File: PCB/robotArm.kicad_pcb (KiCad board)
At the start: 2 copper layers, 85 parts, among them J1 Motor_eje_X, J10 Gripper, J11 Conector Auxiliar 2, J12 5v, J13 End-Stop-X, J14 End-Stop-Y, J15 End-Stop-Z, J16 jumperLed5v, J17 Conector Auxiliar 1, J18 jumperLedVbat, J19 Vbat, J2 3.3v, J20 jumperLedVcc, J21 Vcc, J3 Motor_eje_Y, J4 Motor_eje_Z, J5 micro pasos X, J6 micro pasos Y, J7 micro pasos Z, J8 Conector I2C, J9 jumperLed3.3v, Q1 BC558, Q2 BC558, Q3 BC558, SW1 SW_Push, U1 YAAJ_BluePill, U2 LM7805_TO220, U3 LM317_TO-220

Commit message: PCB pull from master (#12)
* Update README.md

Se agregó descripción,  introducción y fuentes.

* Se consiguió una primera versión de Eje-Stop funcional

* Se inició una interfaz en python sencilla para la comunicación con el robot

* Se comenzó con conexión USB

* Se agregó LCD i2c y lógica de CDC

* update interface

* Se actualizaron los cambios

* return 2025

* El homming funciona!

* modo ejecución v1.0 funciona correctamente

* Se avanzo interfaz 3 modos funcionales v1.0

* actualizaciones en la interfaz

* Recuperando cambios del stash

* Se recuperaron las modificaciones de interfaz

* Se agregó leds en interfaz, botón de limpiar aprendizaje, se arregló configuración de velocidad en bluepill

* readme de stm32

* Se actualizo interfaz v1.0

* Se agregó rampa de velocidad

---------

Co-authored-by: Francisco Cano <100385537+FranciscoCano2@users.noreply.github.com>
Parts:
- removed C1: 103, Capacitor_THT:C_Disc_D8.0mm_W2.5mm_P5.00mm
- removed C6: 470uF, Capacitor_THT:CP_Radial_D8.0mm_P3.80mm
- removed D12: LED_Vbat, LED_THT:LED_D5.0mm
- removed D13, D4, D5, D6, D7, D8, D9: 1N4007, Diode_THT:D_DO-41_SOD81_P10.16mm_Horizontal
- removed J19: Vbat, TerminalBlock:TerminalBlock_bornier-2_P5.08mm
- removed R10: 220, Resistor_THT:R_Axial_DIN0207_L6.3mm_D2.5mm_P10.16mm_Horizontal
- added C19: 103, Capacitor_THT:C_Disc_D8.0mm_W2.5mm_P5.00mm, F.Cu at (166.5, 100.0)
- added C20: 103, Capacitor_THT:C_Disc_D8.0mm_W2.5mm_P5.00mm, F.Cu at (179.0, 98.0)
- added H1: MountingHole, MountingHole:MountingHole_3.2mm_M3_DIN965, F.Cu at (258.5, 42.5)
- added H2: MountingHole, MountingHole:MountingHole_3.2mm_M3_DIN965, F.Cu at (165.0, 40.5)
- added H3: MountingHole, MountingHole:MountingHole_3.2mm_M3_DIN965, F.Cu at (258.5, 134.0)
- added H4: MountingHole, MountingHole:MountingHole_3.2mm_M3_DIN965, F.Cu at (166.0, 135.0)
- added R16: 1k, Resistor_THT:R_Axial_DIN0207_L6.3mm_D2.5mm_P10.16mm_Horizontal, F.Cu at (239.3, 101.8)
- added R17: 1k, Resistor_THT:R_Axial_DIN0207_L6.3mm_D2.5mm_P10.16mm_Horizontal, F.Cu at (235.7, 101.7)
- added R18: 1k, Resistor_THT:R_Axial_DIN0207_L6.3mm_D2.5mm_P10.16mm_Horizontal, F.Cu at (232.1, 101.7)
- added R19: 10k, Resistor_THT:R_Axial_DIN0207_L6.3mm_D2.5mm_P10.16mm_Horizontal, F.Cu at (173.1, 93.0)
- added SW2: STOP_EM, Button_Switch_THT:SW_PUSH_6mm_H5mm, F.Cu at (166.6, 106.2)
- C11, C8: value 470uF -> 10uF
- C5: value 47uF -> 10uF
- D1: value 1N4007 -> LED_Home; footprint Diode_THT:D_DO-41_SOD81_P10.16mm_Horizontal -> LED_THT:LED_D5.0mm
- D2: value 1N4007 -> LED_Wait; footprint Diode_THT:D_DO-41_SOD81_P10.16mm_Horizontal -> LED_THT:LED_D5.0mm
- D3: value 1N4007 -> LED_Finish; footprint Diode_THT:D_DO-41_SOD81_P10.16mm_Horizontal -> LED_THT:LED_D5.0mm
- J12, J2: footprint TerminalBlock:TerminalBlock_bornier-2_P5.08mm -> TerminalBlock_Phoenix:TerminalBlock_Phoenix_PT-1,5-2-5.0-H_1x02_P5.00mm_Horizontal
- J18: value jumperLedVbat -> Pulsador Externo; footprint Connector_PinHeader_2.54mm:PinHeader_2x01_P2.54mm_Vertical -> Connector_PinHeader_2.54mm:PinHeader_1x02_P2.54mm_Vertical
- J21: footprint TerminalBlock:TerminalBlock_bornier-2_P5.08mm -> TerminalBlock_Phoenix:TerminalBlock_Phoenix_MKDS-1,5-2_1x02_P5.00mm_Horizontal
- J5, J6, J7: footprint Connector_PinSocket_2.54mm:PinSocket_2x03_P2.54mm_Vertical -> Connector_PinHeader_2.54mm:PinHeader_2x03_P2.54mm_Vertical
- R12, R13, R7: value 10k -> 47k
- R2, R3, R4: value 10k -> 4.7k
- SW1: value SW_Push -> RESET
- moved D1 174.9 mm to (229.9, 132.3), turned to 0 degrees
- moved D2 148.2 mm to (230.0, 118.1), turned to 0 degrees
- moved J9 128.1 mm to (256.1, 119.8), turned to 180 degrees
- moved R5 127.0 mm to (182.0, 69.7), turned to -90 degrees
- moved D3 124.6 mm to (229.9, 125.4), turned to 0 degrees
- moved R7 122.0 mm to (206.4, 128.3)
- moved D10 121.8 mm to (250.5, 120.5), turned to -90 degrees
- moved R1 121.0 mm to (252.7, 116.8)
- moved C5 120.4 mm to (244.5, 123.1)
- moved C7 114.9 mm to (249.9, 127.2), turned to -90 degrees
- moved C9 110.8 mm to (223.6, 133.7)
- moved J16 109.1 mm to (214.3, 126.7)
- moved J2 108.8 mm to (240.3, 132.0), turned to 0 degrees
- moved R2 108.2 mm to (192.0, 59.8)
- moved D11 107.6 mm to (212.8, 121.4)
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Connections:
- A1 pad 10: Net-(A1-Pad10) -> Net-(A1-MS1)
- A1 pad 12: Net-(A1-Pad12) -> Net-(A1-MS3)
- A1 pad 13: Net-(A1-Pad13) -> Net-(A1-~{RESET})
- A1 pad 14: Net-(A1-Pad14) -> Net-(A1-~{RESET})
- A1 pad 9: Net-(A1-Pad9) -> EnableMotor
- A2 pad 10: Net-(A2-Pad10) -> Net-(A2-MS1)
- A2 pad 12: Net-(A2-Pad12) -> Net-(A2-MS3)
- A2 pad 13: Net-(A2-Pad13) -> Net-(A2-~{RESET})
- A2 pad 14: Net-(A2-Pad14) -> Net-(A2-~{RESET})
- A2 pad 9: Net-(A2-Pad9) -> EnableMotor
- A3 pad 10: Net-(A3-Pad10) -> Net-(A3-MS1)
- A3 pad 12: Net-(A3-Pad12) -> Net-(A3-MS3)
- A3 pad 13: Net-(A3-Pad13) -> Net-(A3-~{RESET})
- A3 pad 14: Net-(A3-Pad14) -> Net-(A3-~{RESET})
- A3 pad 9: Net-(A3-Pad9) -> EnableMotor
- D1 pad 1: Net-(A1-Pad9) -> GNDREF
- D1 pad 2: EnableMotor -> Net-(D1-A)
- D18 pad 2: Net-(D18-Pad2) -> Net-(D18-A)
- D2 pad 1: Net-(A2-Pad9) -> GNDREF
- D2 pad 2: EnableMotor -> Net-(D2-A)
- D3 pad 1: Net-(A3-Pad9) -> GNDREF
- D3 pad 2: EnableMotor -> Net-(D3-A)
- J12 pad 1: +5V -> GNDREF
- J12 pad 2: GNDREF -> +5V
- J17 pad 1: +3V3 -> +5V
- J17 pad 2: Net-(J17-Pad2) -> +3V3
- J17 pad 3: Net-(J17-Pad3) -> Net-(J17-Pin_3)
- J17 pad 4: Net-(J17-Pad4) -> Net-(J17-Pin_4)
- J17 pad 5: Net-(J17-Pad5) -> Net-(J17-Pin_5)
- J17 pad 6: Net-(J17-Pad6) -> Net-(J17-Pin_6)
- J17 pad 7: Net-(J17-Pad7) -> Net-(J17-Pin_7)
- J17 pad 8: Net-(J17-Pad8) -> Net-(J17-Pin_8)
- J17 pad 9: Net-(J17-Pad9) -> GNDREF
- J18 pad 1: Net-(D12-Pad2) -> GNDREF
- J18 pad 2: +BATT -> STOP
- J2 pad 1: +3V3 -> GNDREF
- J2 pad 2: GNDREF -> +3V3
- J21 pad 1: GNDREF -> Net-(D18-A)
- J21 pad 2: Net-(D18-Pad2) -> GNDREF
- J5 pad 1: Net-(A1-Pad12) -> Net-(A1-MS1)
- J5 pad 2: GNDREF -> +3V3
- J5 pad 4: GNDREF -> +3V3
- J5 pad 5: Net-(A1-Pad10) -> Net-(A1-MS3)
- J5 pad 6: GNDREF -> +3V3
- J6 pad 1: Net-(A2-Pad12) -> Net-(A2-MS1)
- J6 pad 2: GNDREF -> +3V3
- J6 pad 4: GNDREF -> +3V3
- J6 pad 5: Net-(A2-Pad10) -> Net-(A2-MS3)
- J6 pad 6: GNDREF -> +3V3
- J7 pad 1: Net-(A3-Pad12) -> Net-(A3-MS1)
- J7 pad 2: GNDREF -> +3V3
- J7 pad 4: GNDREF -> +3V3
- J7 pad 5: Net-(A3-Pad10) -> Net-(A3-MS3)
- J7 pad 6: GNDREF -> +3V3
- J8 pad 1: +3V3 -> +5V
- R12 pad 1: StopX -> StopY
- R12 pad 2: GNDREF -> +3V3
- R13 pad 2: GNDREF -> +3V3
- R2 pad 2: Net-(A1-Pad13) -> Net-(A1-~{RESET})
- R3 pad 2: Net-(A2-Pad13) -> Net-(A2-~{RESET})
- R4 pad 2: Net-(A3-Pad13) -> Net-(A3-~{RESET})
- R7 pad 1: StopY -> StopX
- R7 pad 2: GNDREF -> +3V3
- U1 pad 10: Net-(J17-Pad4) -> Net-(J17-Pin_3)
- U1 pad 11: Net-(J17-Pad3) -> home
- U1 pad 12: Net-(J17-Pad2) -> finish
- U1 pad 13: SleepMotor -> wait
- U1 pad 21: +BATT -> unconnected-(U1-VBat-Pad21)
- U1 pad 22: Net-(U1-Pad22) -> unconnected-(U1-PC13-Pad22)
- U1 pad 23: Net-(U1-Pad23) -> unconnected-(U1-PC14-Pad23)
- U1 pad 24: Net-(U1-Pad24) -> unconnected-(U1-PC15-Pad24)
- U1 pad 4: ResetMotor -> STOP
- U1 pad 5: Net-(J17-Pad9) -> Net-(J17-Pin_8)
- U1 pad 6: Net-(J17-Pad8) -> Net-(J17-Pin_7)
- U1 pad 7: Net-(J17-Pad7) -> Net-(J17-Pin_6)
- U1 pad 8: Net-(J17-Pad6) -> Net-(J17-Pin_5)
- U1 pad 9: Net-(J17-Pad5) -> Net-(J17-Pin_4)
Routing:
- net SleepMotor: track 126.1 -> 0.00 mm
- net ResetMotor: track 91.6 -> 0.00 mm
- net +BATT: track 57.5 -> 0.00 mm, vias 2 -> 0
- net STOP: track 0.00 -> 49.5 mm
- net home: track 0.00 -> 46.4 mm
- net finish: track 0.00 -> 37.4 mm
- net Net-(A2-Pad13): track 35.7 -> 0.00 mm
- net Net-(U1-RST): track 27.5 -> 57.6 mm
- net Net-(A3-Pad13): track 28.2 -> 0.00 mm
- net wait: track 0.00 -> 28.0 mm
- net Net-(D1-A): track 0.00 -> 23.2 mm
- net DirZ: track 80.8 -> 58.0 mm
- net Net-(D3-A): track 0.00 -> 14.8 mm
- net Net-(A1-Pad13): track 13.7 -> 0.00 mm
- net Net-(A2-MS1): track 0.00 -> 9.79 mm
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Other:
- board outline added: 100 x 100 mm
- net class Default removed
- board text added: "V:1.6 F:12/10/2023"
- board text removed: "V:1.0 F:22/6/2023"

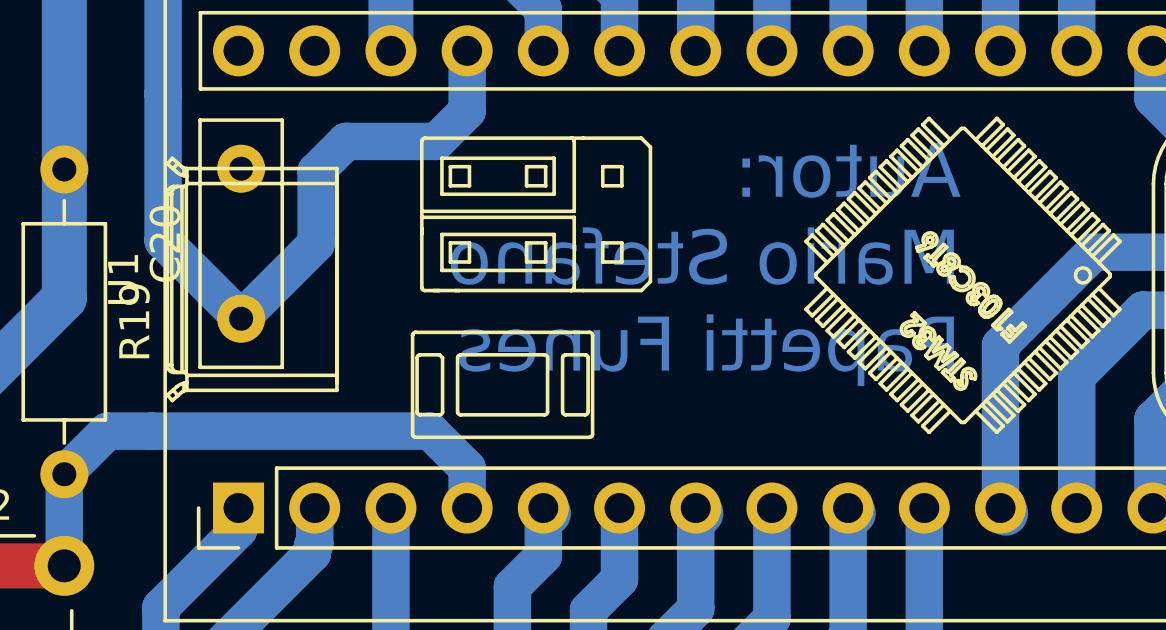
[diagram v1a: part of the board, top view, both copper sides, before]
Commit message: Limpieza: Eliminación de archivos temporales de KiCad
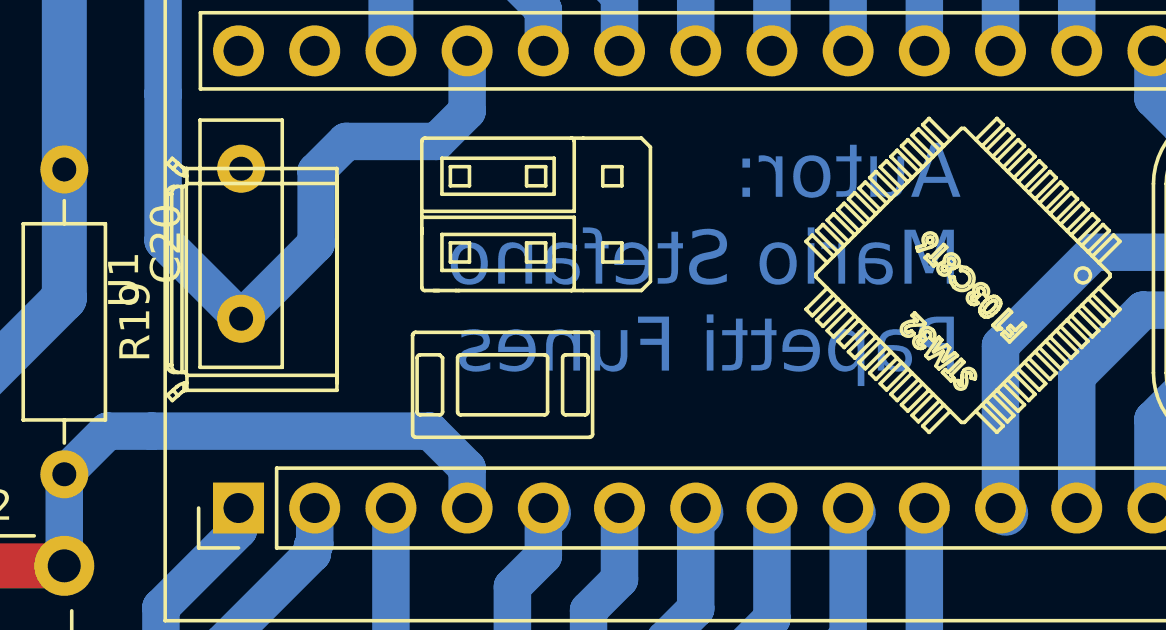
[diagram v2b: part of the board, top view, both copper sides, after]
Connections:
- J13 pad 1: StopX -> StopZ
- J15 pad 1: StopZ -> StopX
- Q1 pad 2: StopX -> StopZ
- Q3 pad 2: StopZ -> StopX
- R13 pad 1: StopZ -> StopX
- R7 pad 1: StopX -> StopZ
- U1 pad 1: StopZ -> StopX
- U1 pad 3: StopX -> StopZ
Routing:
- net StopZ: track 42.5 -> 52.9 mm
- net StopX: track 52.9 -> 42.5 mm
